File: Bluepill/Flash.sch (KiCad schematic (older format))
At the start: 50 parts, among them CON1 GENESIS-CONN, J1 USB_B_Micro, J2 Conn_Bluepill_Left, J3 Conn_Bluepill_right, U1 RT9193, U2 STM32F103C8Tx, U3 4069, U4 74HC590, U5 74LVC245, U6 74HC590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

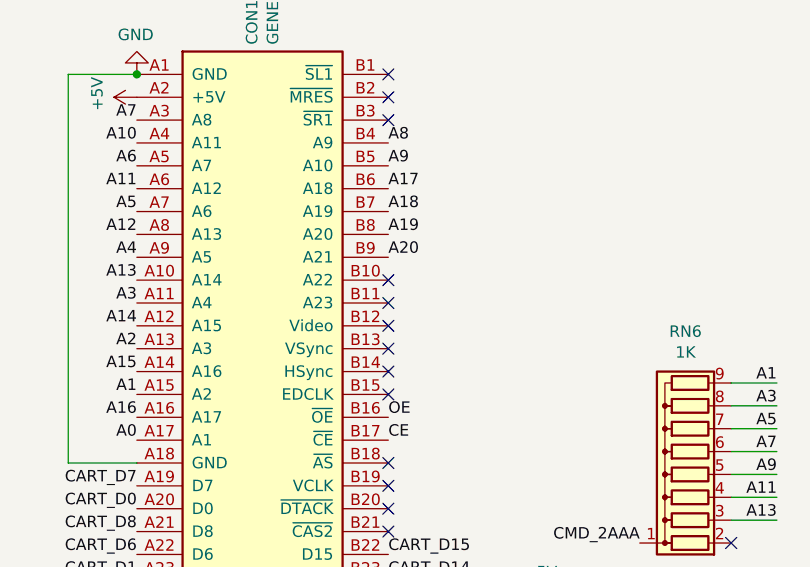
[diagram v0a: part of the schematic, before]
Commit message: Connected A22 and A23 on the cart connector for SNES support
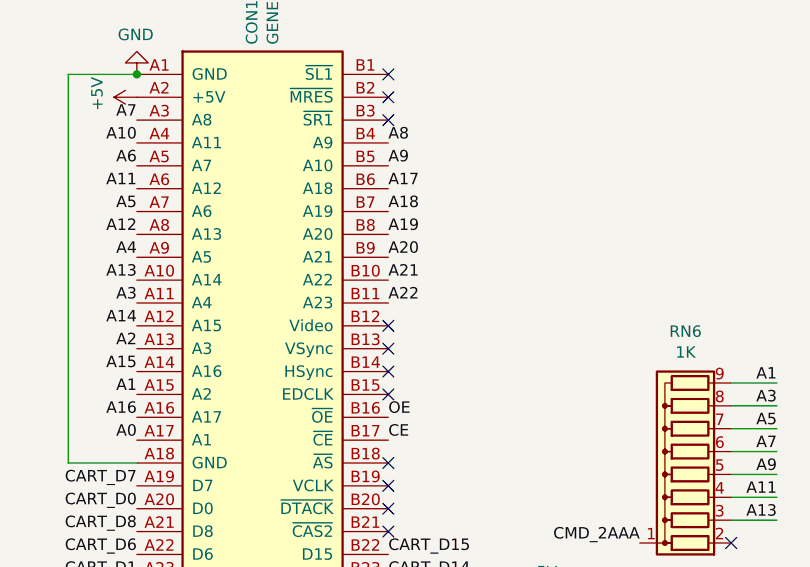
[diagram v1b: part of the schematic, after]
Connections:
- net A21: now also CON1.B10 (A22)
- net A22: now also CON1.B11 (A23)
- no-connect marks 33 -> 31
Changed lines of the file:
@@
 NoConn ~ 14200 3600
 NoConn ~ 14200 3500
-NoConn ~ 14200 3400
-NoConn ~ 14200 3300
 NoConn ~ 14200 2600
 NoConn ~ 14200 2500
@@
 NoConn ~ 6400 7650
 NoConn ~ 6400 7750
+Text Label 14200 3300 0    50   ~ 0
+A21
+Text Label 14200 3400 0    50   ~ 0
+A22
 $EndSCHEMATC
